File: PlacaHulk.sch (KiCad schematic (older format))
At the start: 7 parts, among them U1 MAX232

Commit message: adicionei PCB
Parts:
- C1: footprint (none) -> Capacitor_THT:CP_Radial_D5.0mm_P2.50mm
- C2, C3, C4: renamed from C?; footprint (none) -> Capacitor_THT:CP_Radial_D5.0mm_P2.50mm
- J1: renamed from J?; footprint (none) -> Connector_PinSocket_2.54mm:PinSocket_1x03_P2.54mm_Vertical
- J2: renamed from J?; footprint (none) -> Connector_Dsub:DSUB-25_Female_Vertical_P2.77x2.84mm
- U1: footprint (none) -> Package_DIP:DIP-16_W7.62mm
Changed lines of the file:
@@
 F 0 "U1" H 4200 4181 50  0000 C CNN
 F 1 "MAX232" H 4200 4090 50  0000 C CNN
-F 2 "" H 4250 1750 50  0001 L CNN
+F 2 "Package_DIP:DIP-16_W7.62mm" H 4250 1750 50  0001 L CNN
 F 3 "http://www.ti.com/lit/ds/symlink/max232.pdf" H 4200 2900 50  0001 C CNN
 	1    4200 2800
@@
 F 0 "C1" H 5928 2396 50  0000 L CNN
 F 1 "CAP" H 5928 2305 50  0000 L CNN
-F 2 "" H 5750 2350 50  0001 C CNN
+F 2 "Capacitor_THT:CP_Radial_D5.0mm_P2.50mm" H 5750 2350 50  0001 C CNN
 F 3 "~" H 5750 2350 50  0001 C CNN
 	1    5750 2350
@@
 $EndComp
 $Comp
-L Connector:DB25_Female J?
+L Connector:DB25_Female J2
 U 1 1 5E4574EF
 P 7800 3000
-F 0 "J?" H 7980 3046 50  0000 L CNN
+F 0 "J2" H 7980 3046 50  0000 L CNN
 F 1 "DB25_Female" H 7980 2955 50  0000 L CNN
-F 2 "" H 7800 3000 50  0001 C CNN
+F 2 "Connector_Dsub:DSUB-25_Female_Vertical_P2.77x2.84mm" H 7800 3000 50  0001 C CNN
 F 3 " ~" H 7800 3000 50  0001 C CNN
 	1    7800 3000
@@
 $EndComp
 $Comp
-L power:GND #PWR?
+L power:GND #PWR05
 U 1 1 5E474845
 P 6800 2700
-F 0 "#PWR?" H 6800 2450 50  0001 C CNN
+F 0 "#PWR05" H 6800 2450 50  0001 C CNN
 F 1 "GND" H 6805 2527 50  0000 C CNN
 F 2 "" H 6800 2700 50  0001 C CNN
@@
 	4250 4000 4200 4000
 $Comp
-L pspice:CAP C?
+L pspice:CAP C2
 U 1 1 5E487C7B
 P 2650 2000
-F 0 "C?" H 2828 2046 50  0000 L CNN
+F 0 "C2" H 2828 2046 50  0000 L CNN
 F 1 "CAP" H 2828 1955 50  0000 L CNN
-F 2 "" H 2650 2000 50  0001 C CNN
+F 2 "Capacitor_THT:CP_Radial_D5.0mm_P2.50mm" H 2650 2000 50  0001 C CNN
 F 3 "~" H 2650 2000 50  0001 C CNN
 	1    2650 2000
@@
 	3400 2250 3400 2200
 $Comp
-L power:GND #PWR?
+L power:GND #PWR01
 U 1 1 5E46B6EB
 P 4200 4200
-F 0 "#PWR?" H 4200 3950 50  0001 C CNN
+F 0 "#PWR01" H 4200 3950 50  0001 C CNN
 F 1 "GND" H 4205 4027 50  0000 C CNN
 F 2 "" H 4200 4200 50  0001 C CNN
@@
 	5000 2900 6450 2900
 $Comp
-L pspice:CAP C?
+L pspice:CAP C4
 U 1 1 5E4A2D2D
 P 6150 2350
-F 0 "C?" H 6328 2396 50  0000 L CNN
+F 0 "C4" H 6328 2396 50  0000 L CNN
 F 1 "CAP" H 6328 2305 50  0000 L CNN
-F 2 "" H 6150 2350 50  0001 C CNN
+F 2 "Capacitor_THT:CP_Radial_D5.0mm_P2.50mm" H 6150 2350 50  0001 C CNN
 F 3 "~" H 6150 2350 50  0001 C CNN
 	1    6150 2350
@@
 $EndComp
 $Comp
-L pspice:CAP C?
+L pspice:CAP C3
 U 1 1 5E4A9677
 P 5400 2350
-F 0 "C?" H 5578 2396 50  0000 L CNN
+F 0 "C3" H 5578 2396 50  0000 L CNN
 F 1 "CAP" H 5578 2305 50  0000 L CNN
-F 2 "" H 5400 2350 50  0001 C CNN
+F 2 "Capacitor_THT:CP_Radial_D5.0mm_P2.50mm" H 5400 2350 50  0001 C CNN
 F 3 "~" H 5400 2350 50  0001 C CNN
 	1    5400 2350
@@
 	6150 1950 6150 2100
 $Comp
-L power:GND #PWR?
+L power:GND #PWR02
 U 1 1 5E4ADDCB
 P 5400 2600
-F 0 "#PWR?" H 5400 2350 50  0001 C CNN
+F 0 "#PWR02" H 5400 2350 50  0001 C CNN
 F 1 "GND" H 5405 2427 50  0000 C CNN
 F 2 "" H 5400 2600 50  0001 C CNN
@@
 $EndComp
 $Comp
-L power:+5V #PWR?
+L power:+5V #PWR04
 U 1 1 5E4AFAB5
 P 5850 2700
-F 0 "#PWR?" H 5850 2550 50  0001 C CNN
+F 0 "#PWR04" H 5850 2550 50  0001 C CNN
 F 1 "+5V" H 5865 2873 50  0000 C CNN
 F 2 "" H 5850 2700 50  0001 C CNN
@@
 	5850 2750 5850 2700
 $Comp
-L power:+5V #PWR?
+L power:+5V #PWR03
 U 1 1 5E4B0D24
 P 5500 1450
-F 0 "#PWR?" H 5500 1300 50  0001 C CNN
+F 0 "#PWR03" H 5500 1300 50  0001 C CNN
 F 1 "+5V" H 5515 1623 50  0000 C CNN
 F 2 "" H 5500 1450 50  0001 C CNN
@@
 Connection ~ 5500 1600
 $Comp
-L Connector_Generic:Conn_01x03 J?
+L Connector_Generic:Conn_01x03 J1
 U 1 1 5E4BCB35
 P 2450 3150
-F 0 "J?" H 2530 3192 50  0000 L CNN
+F 0 "J1" H 2530 3192 50  0000 L CNN
 F 1 "Conn_01x03" H 2530 3101 50  0000 L CNN
-F 2 "" H 2450 3150 50  0001 C CNN
+F 2 "Connector_PinSocket_2.54mm:PinSocket_1x03_P2.54mm_Vertical" H 2450 3150 50  0001 C CNN
 F 3 "~" H 2450 3150 50  0001 C CNN
 	1    2450 3150

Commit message: Feito o layout da PCB.
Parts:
- removed J1: Conn_01x03, Connector_PinSocket_2.54mm:PinSocket_1x03_P2.54mm_Vertical, symbol Connector_Generic:Conn_01x03
- added J1: Conn_01x04, Connector_PinSocket_2.54mm:PinSocket_1x04_P2.54mm_Vertical, symbol Connector_Generic:Conn_01x04
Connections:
- net +5V: now also J1.1 (Pin_1)
- net GND: now also J2.13, J2.9, J1.4 (Pin_4)
- net at U1.11 (T1IN): now also J1.2 (Pin_2)
- net at U1.12 (R1OUT): now also J1.3 (Pin_3)
- net +5C: now reaches J2.25 (P25)
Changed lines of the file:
@@
 $EndComp
 Wire Wire Line
-	6800 2700 7300 2700
+	6800 2700 7000 2700
 Wire Wire Line
 	7300 2700 7300 2600
@@
 	5500 1450 5500 1600
 Connection ~ 5500 1600
-$Comp
-L Connector_Generic:Conn_01x03 J1
-U 1 1 5E4BCB35
-P 2450 3150
-F 0 "J1" H 2530 3192 50  0000 L CNN
-F 1 "Conn_01x03" H 2530 3101 50  0000 L CNN
-F 2 "Connector_PinSocket_2.54mm:PinSocket_1x03_P2.54mm_Vertical" H 2450 3150 50  0001 C CNN
-F 3 "~" H 2450 3150 50  0001 C CNN
-	1    2450 3150
-	-1   0    0    1
-$EndComp
-Wire Wire Line
-	2650 3250 3050 3250
 Wire Wire Line
 	3050 3250 3050 4000
@@
 	3050 4000 4200 4000
 Wire Wire Line
-	2650 3150 3250 3150
-Wire Wire Line
 	3250 3150 3250 3300
 Wire Wire Line
 	3250 3300 3400 3300
 Wire Wire Line
-	2650 3050 3000 3050
-Wire Wire Line
 	3000 3050 3000 2900
 Wire Wire Line
 	3000 2900 3400 2900
+$Comp
+L Connector_Generic:Conn_01x04 J1
+U 1 1 5E46CB90
+P 2200 3050
+F 0 "J1" H 2118 3367 50  0000 C CNN
+F 1 "Conn_01x04" H 2118 3276 50  0000 C CNN
+F 2 "Connector_PinSocket_2.54mm:PinSocket_1x04_P2.54mm_Vertical" H 2200 3050 50  0001 C CNN
+F 3 "~" H 2200 3050 50  0001 C CNN
+	1    2200 3050
+	-1   0    0    -1
+$EndComp
+Wire Wire Line
+	2400 3250 3050 3250
+Wire Wire Line
+	2400 3150 3250 3150
+Wire Wire Line
+	2400 3050 3000 3050
+Wire Wire Line
+	2400 2950 2400 1650
+Wire Wire Line
+	2400 1650 2500 1650
+Wire Wire Line
+	2500 1650 2500 1600
+Wire Wire Line
+	2500 1600 4200 1600
+Connection ~ 4200 1600
+Wire Wire Line
+	7000 4200 7000 3400
+Connection ~ 7000 2700
+Wire Wire Line
+	7000 2700 7300 2700
+Wire Wire Line
+	7500 3400 7000 3400
+Connection ~ 7000 3400
+Wire Wire Line
+	7000 3400 7000 2700
+$Comp
+L power:+5C #PWR?
+U 1 1 5E488E1B
+P 7250 3650
+F 0 "#PWR?" H 7250 3500 50  0001 C CNN
+F 1 "+5C" H 7265 3823 50  0000 C CNN
+F 2 "" H 7250 3650 50  0001 C CNN
+F 3 "" H 7250 3650 50  0001 C CNN
+	1    7250 3650
+	1    0    0    -1
+$EndComp
+Wire Wire Line
+	7500 4200 7000 4200
+Wire Wire Line
+	7500 4100 7250 4100
+Wire Wire Line
+	7250 4100 7250 3650
 $EndSCHEMATC

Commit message: Mudado os pinos usados e o layout da PCB.
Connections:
- net +5V is gone; now on net +5C: C1.2, J1.1 (Pin_1), J2.14 (P14), U1.16 (VCC)
- net GND: now also J2.1
- net at U1.10 (T2IN): now also J1.2 (Pin_2)
- net at U1.11 (T1IN): no longer J1.2 (Pin_2)
- net at U1.12 (R1OUT): no longer J1.3 (Pin_3)
- net at U1.13 (R1IN): no longer J2.2
- net at U1.14 (T1OUT): no longer J2.3
- net at U1.7 (T2OUT): now also J2.3
- net at U1.8 (R2IN): now also J2.2
- net at U1.9 (R2OUT): now also J1.3 (Pin_3)
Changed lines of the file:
@@
 	7300 2600 7500 2600
 Wire Wire Line
-	7500 1900 5500 1900
+	7500 1900 6550 1900
 Wire Wire Line
 	5500 1900 5500 1600
@@
 	4200 4000 4200 4200
 Connection ~ 4200 4000
-Wire Wire Line
-	6500 2000 7500 2000
-Wire Wire Line
-	6450 2200 7500 2200
-Wire Wire Line
-	6500 3300 6500 2000
-Wire Wire Line
-	5000 3300 6500 3300
-Wire Wire Line
-	6450 2900 6450 2200
-Wire Wire Line
-	5000 2900 6450 2900
 $Comp
 L pspice:CAP C4
@@
 Wire Wire Line
 	3050 4000 4200 4000
-Wire Wire Line
-	3250 3150 3250 3300
-Wire Wire Line
-	3250 3300 3400 3300
-Wire Wire Line
-	3000 3050 3000 2900
-Wire Wire Line
-	3000 2900 3400 2900
 $Comp
 L Connector_Generic:Conn_01x04 J1
@@
 	2400 3250 3050 3250
 Wire Wire Line
-	2400 3150 3250 3150
-Wire Wire Line
-	2400 3050 3000 3050
-Wire Wire Line
 	2400 2950 2400 1650
 Wire Wire Line
@@
 	7000 3400 7000 2700
 $Comp
-L power:+5C #PWR?
+L power:+5C #PWR0101
 U 1 1 5E488E1B
 P 7250 3650
-F 0 "#PWR?" H 7250 3500 50  0001 C CNN
+F 0 "#PWR0101" H 7250 3500 50  0001 C CNN
 F 1 "+5C" H 7265 3823 50  0000 C CNN
 F 2 "" H 7250 3650 50  0001 C CNN
@@
 	7500 4100 7250 4100
 Wire Wire Line
-	7250 4100 7250 3650
+	7250 4100 7250 3700
+$Comp
+L power:GND #PWR0102
+U 1 1 5E4AE3AD
+P 7100 1650
+F 0 "#PWR0102" H 7100 1400 50  0001 C CNN
+F 1 "GND" H 7105 1477 50  0000 C CNN
+F 2 "" H 7100 1650 50  0001 C CNN
+F 3 "" H 7100 1650 50  0001 C CNN
+	1    7100 1650
+	1    0    0    -1
+$EndComp
+Wire Wire Line
+	7100 1650 7500 1650
+Wire Wire Line
+	7500 1650 7500 1800
+Wire Wire Line
+	7250 3700 6650 3700
+Wire Wire Line
+	6650 3700 6650 4600
+Wire Wire Line
+	6650 4600 8300 4600
+Wire Wire Line
+	8300 4600 8300 1450
+Wire Wire Line
+	8300 1450 6550 1450
+Wire Wire Line
+	6550 1450 6550 1900
+Connection ~ 7250 3700
+Wire Wire Line
+	7250 3700 7250 3650
+Connection ~ 6550 1900
+Wire Wire Line
+	6550 1900 5500 1900
+Wire Wire Line
+	6450 2200 7500 2200
+Wire Wire Line
+	6500 2000 7500 2000
+Wire Wire Line
+	2400 3050 3400 3050
+Wire Wire Line
+	3400 3050 3400 3100
+Wire Wire Line
+	2400 3150 3300 3150
+Wire Wire Line
+	3300 3150 3300 3500
+Wire Wire Line
+	3300 3500 3400 3500
+Wire Wire Line
+	5000 3500 6500 3500
+Wire Wire Line
+	6500 2000 6500 3500
+Wire Wire Line
+	5000 3100 6450 3100
+Wire Wire Line
+	6450 2200 6450 3100
 $EndSCHEMATC

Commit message: Adicionado os conectores do encoder.
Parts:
- added J?: Conn_01x04, symbol Connector_Generic:Conn_01x04
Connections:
- net at J2.11: now also J?.2 (Pin_2)
- net at J2.12: now also J?.4 (Pin_4)
- net at J2.23 (P23): now also J?.1 (Pin_1)
- net at J2.24 (P24): now also J?.3 (Pin_3)
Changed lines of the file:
@@
 Wire Wire Line
 	6450 2200 6450 3100
+Wire Wire Line
+	7500 3700 7350 3700
+Wire Wire Line
+	7350 3700 7350 3750
+Wire Wire Line
+	7350 3750 6050 3750
+Wire Wire Line
+	6050 3850 7350 3850
+Wire Wire Line
+	7350 3850 7350 3800
+Wire Wire Line
+	7350 3800 7500 3800
+Wire Wire Line
+	6050 4050 7350 4050
+Wire Wire Line
+	7350 4050 7350 4000
+Wire Wire Line
+	7350 4000 7500 4000
+$Comp
+L Connector_Generic:Conn_01x04 J?
+U 1 1 5E4F10B5
+P 5850 3850
+F 0 "J?" H 5768 4167 50  0000 C CNN
+F 1 "Conn_01x04" H 5768 4076 50  0000 C CNN
+F 2 "" H 5850 3850 50  0001 C CNN
+F 3 "~" H 5850 3850 50  0001 C CNN
+	1    5850 3850
+	-1   0    0    -1
+$EndComp
+Wire Wire Line
+	6050 3950 7350 3950
+Wire Wire Line
+	7350 3950 7350 3900
+Wire Wire Line
+	7350 3900 7500 3900
 $EndSCHEMATC

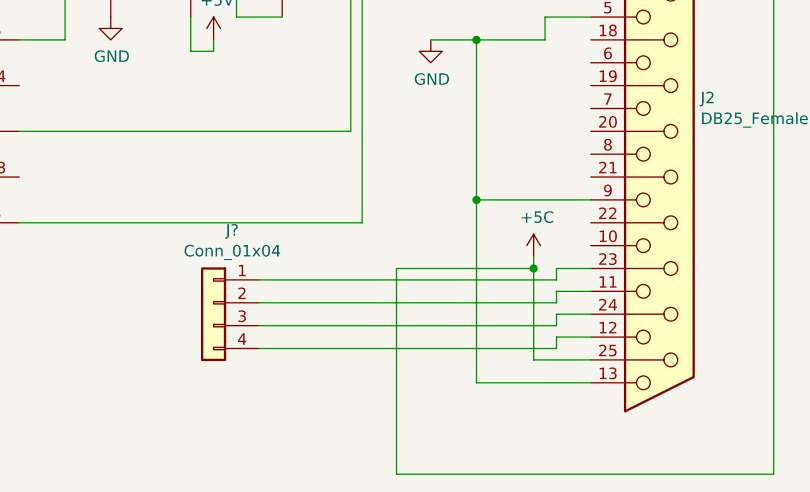
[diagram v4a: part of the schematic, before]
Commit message: Refeito o layout da Placa com os conectores do encoder.
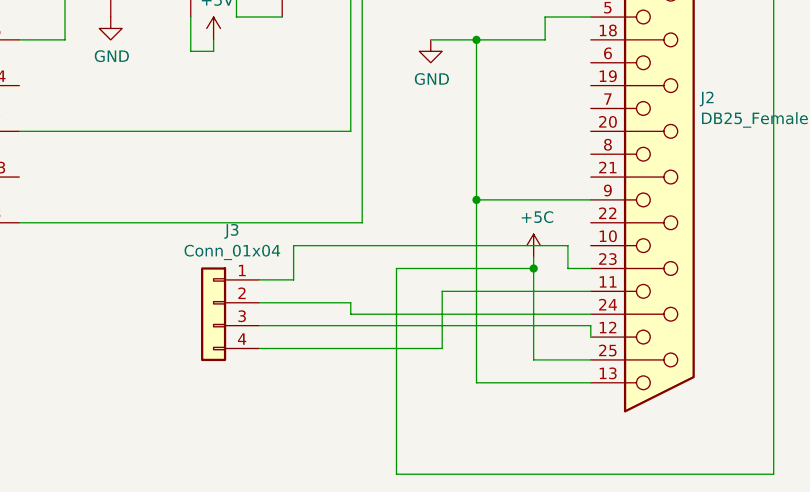
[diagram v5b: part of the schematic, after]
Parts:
- J3: renamed from J?; footprint (none) -> Connector_PinSocket_2.54mm:PinSocket_1x04_P2.54mm_Vertical
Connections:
- net at J2.11: now also J3.4 (Pin_4); no longer J3.2 (Pin_2)
- net at J2.12: now also J3.3 (Pin_3); no longer J3.4 (Pin_4)
- net at J2.24 (P24): now also J3.2 (Pin_2); no longer J3.3 (Pin_3)
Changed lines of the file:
@@
-$EndComp
-$Comp
-L Connector:DB25_Female J2
-U 1 1 5E4574EF
-P 7800 3000
-F 0 "J2" H 7980 3046 50  0000 L CNN
-F 1 "DB25_Female" H 7980 2955 50  0000 L CNN
-F 2 "Connector_Dsub:DSUB-25_Female_Vertical_P2.77x2.84mm" H 7800 3000 50  0001 C CNN
-F 3 " ~" H 7800 3000 50  0001 C CNN
-	1    7800 3000
-	1    0    0    -1
 $EndComp
 $Comp
@@
 Wire Wire Line
 	7000 3400 7000 2700
+Wire Wire Line
+	7500 4200 7000 4200
+Wire Wire Line
+	7500 4100 7250 4100
+Wire Wire Line
+	7250 4100 7250 3700
+$Comp
+L power:GND #PWR0102
+U 1 1 5E4AE3AD
+P 7100 1650
+F 0 "#PWR0102" H 7100 1400 50  0001 C CNN
+F 1 "GND" H 7105 1477 50  0000 C CNN
+F 2 "" H 7100 1650 50  0001 C CNN
+F 3 "" H 7100 1650 50  0001 C CNN
+	1    7100 1650
+	1    0    0    -1
+$EndComp
+Wire Wire Line
+	7100 1650 7500 1650
+Wire Wire Line
+	7500 1650 7500 1800
+Wire Wire Line
+	7250 3700 6650 3700
+Wire Wire Line
+	6650 3700 6650 4600
+Wire Wire Line
+	6650 4600 8300 4600
+Wire Wire Line
+	8300 4600 8300 1450
+Wire Wire Line
+	8300 1450 6550 1450
+Wire Wire Line
+	6550 1450 6550 1900
+Connection ~ 7250 3700
+Wire Wire Line
+	7250 3700 7250 3650
+Connection ~ 6550 1900
+Wire Wire Line
+	6550 1900 5500 1900
+Wire Wire Line
+	6450 2200 7500 2200
+Wire Wire Line
+	6500 2000 7500 2000
+Wire Wire Line
+	2400 3050 3400 3050
+Wire Wire Line
+	3400 3050 3400 3100
+Wire Wire Line
+	2400 3150 3300 3150
+Wire Wire Line
+	3300 3150 3300 3500
+Wire Wire Line
+	3300 3500 3400 3500
+Wire Wire Line
+	5000 3500 6500 3500
+Wire Wire Line
+	6500 2000 6500 3500
+Wire Wire Line
+	5000 3100 6450 3100
+Wire Wire Line
+	6450 2200 6450 3100
+$Comp
+L Connector_Generic:Conn_01x04 J3
+U 1 1 5E4F10B5
+P 5850 3850
+F 0 "J3" H 5768 4167 50  0000 C CNN
+F 1 "Conn_01x04" H 5768 4076 50  0000 C CNN
+F 2 "Connector_PinSocket_2.54mm:PinSocket_1x04_P2.54mm_Vertical" H 5850 3850 50  0001 C CNN
+F 3 "~" H 5850 3850 50  0001 C CNN
+	1    5850 3850
+	-1   0    0    -1
+$EndComp
 $Comp
 L power:+5C #PWR0101
@@
 	1    0    0    -1
 $EndComp
-Wire Wire Line
-	7500 4200 7000 4200
-Wire Wire Line
-	7500 4100 7250 4100
-Wire Wire Line
-	7250 4100 7250 3700
-$Comp
-L power:GND #PWR0102
-U 1 1 5E4AE3AD
-P 7100 1650
-F 0 "#PWR0102" H 7100 1400 50  0001 C CNN
-F 1 "GND" H 7105 1477 50  0000 C CNN
-F 2 "" H 7100 1650 50  0001 C CNN
-F 3 "" H 7100 1650 50  0001 C CNN
-	1    7100 1650
-	1    0    0    -1
-$EndComp
-Wire Wire Line
-	7100 1650 7500 1650
-Wire Wire Line
-	7500 1650 7500 1800
-Wire Wire Line
-	7250 3700 6650 3700
-Wire Wire Line
-	6650 3700 6650 4600
-Wire Wire Line
-	6650 4600 8300 4600
-Wire Wire Line
-	8300 4600 8300 1450
-Wire Wire Line
-	8300 1450 6550 1450
-Wire Wire Line
-	6550 1450 6550 1900
-Connection ~ 7250 3700
-Wire Wire Line
-	7250 3700 7250 3650
-Connection ~ 6550 1900
-Wire Wire Line
-	6550 1900 5500 1900
-Wire Wire Line
-	6450 2200 7500 2200
-Wire Wire Line
-	6500 2000 7500 2000
-Wire Wire Line
-	2400 3050 3400 3050
-Wire Wire Line
-	3400 3050 3400 3100
-Wire Wire Line
-	2400 3150 3300 3150
-Wire Wire Line
-	3300 3150 3300 3500
-Wire Wire Line
-	3300 3500 3400 3500
-Wire Wire Line
-	5000 3500 6500 3500
-Wire Wire Line
-	6500 2000 6500 3500
-Wire Wire Line
-	5000 3100 6450 3100
-Wire Wire Line
-	6450 2200 6450 3100
-Wire Wire Line
-	7500 3700 7350 3700
-Wire Wire Line
-	7350 3700 7350 3750
-Wire Wire Line
-	7350 3750 6050 3750
-Wire Wire Line
-	6050 3850 7350 3850
-Wire Wire Line
-	7350 3850 7350 3800
-Wire Wire Line
-	7350 3800 7500 3800
-Wire Wire Line
-	6050 4050 7350 4050
-Wire Wire Line
-	7350 4050 7350 4000
-Wire Wire Line
-	7350 4000 7500 4000
-$Comp
-L Connector_Generic:Conn_01x04 J?
-U 1 1 5E4F10B5
-P 5850 3850
-F 0 "J?" H 5768 4167 50  0000 C CNN
-F 1 "Conn_01x04" H 5768 4076 50  0000 C CNN
-F 2 "" H 5850 3850 50  0001 C CNN
-F 3 "~" H 5850 3850 50  0001 C CNN
-	1    5850 3850
-	-1   0    0    -1
-$EndComp
-Wire Wire Line
-	6050 3950 7350 3950
-Wire Wire Line
-	7350 3950 7350 3900
-Wire Wire Line
-	7350 3900 7500 3900
+$Comp
+L Connector:DB25_Female J2
+U 1 1 5E4574EF
+P 7800 3000
+F 0 "J2" H 7980 3046 50  0000 L CNN
+F 1 "DB25_Female" H 7980 2955 50  0000 L CNN
+F 2 "Connector_Dsub:DSUB-25_Female_Vertical_P2.77x2.84mm" H 7800 3000 50  0001 C CNN
+F 3 " ~" H 7800 3000 50  0001 C CNN
+	1    7800 3000
+	1    0    0    -1
+$EndComp
+Wire Wire Line
+	7500 3700 7400 3700
+Wire Wire Line
+	7400 3700 7400 3600
+Wire Wire Line
+	7400 3600 6200 3600
+Wire Wire Line
+	6200 3600 6200 3750
+Wire Wire Line
+	6200 3750 6050 3750
+Wire Wire Line
+	7500 3900 6450 3900
+Wire Wire Line
+	6450 3900 6450 3850
+Wire Wire Line
+	6450 3850 6050 3850
+Wire Wire Line
+	7500 3800 6850 3800
+Wire Wire Line
+	6850 3800 6850 4050
+Wire Wire Line
+	6850 4050 6050 4050
+Wire Wire Line
+	6050 3950 7500 3950
+Wire Wire Line
+	7500 3950 7500 4000
 $EndSCHEMATC
